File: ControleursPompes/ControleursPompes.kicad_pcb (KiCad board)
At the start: 4 copper layers, 90.8 x 49.5 mm, 91 parts, among them J1 SWD, J10 EV, J11 VACUOSTAT, J12 PV, J13 EV, J14 VACUOSTAT, J15 PV, J16 EV, J17 VACUOSTAT, J2 PWR_IN, J3 I2C 5V, J4 I2C 3.3V, J5 ARIG Interf, J6 PV, J7 EV, J8 VACUOSTAT, J9 PV, Q1 BSS138, Q2 BSS138, SW1 Reset, SW2 Reset, SW3 Reset, U1 AMS1117-3.3, U2 STM32F103C8Tx, U3 TB6612FNG, U4 TB6612FNG, U5 TB6612FNG, U6 TB6612FNG, Y1 16Mhz

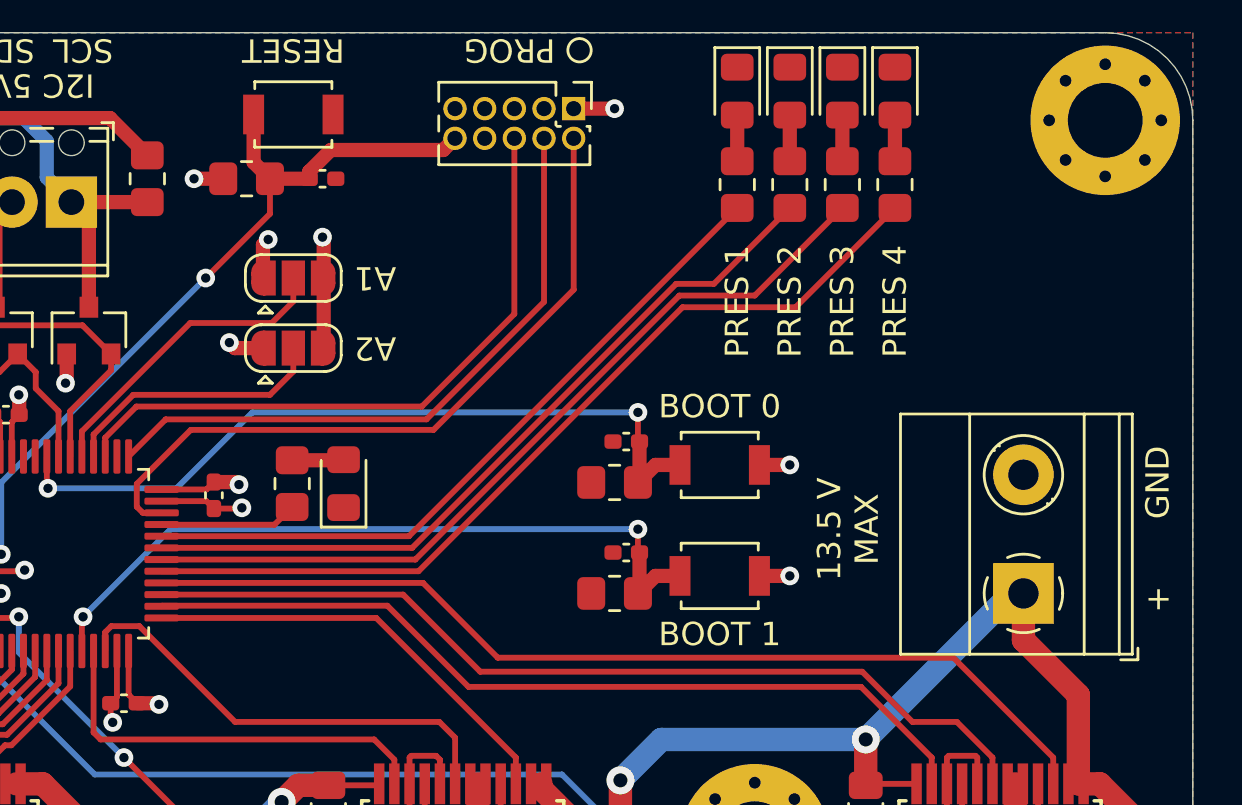
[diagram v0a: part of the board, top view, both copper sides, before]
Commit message: Ajout bornier alim 5V sur controleur pompes
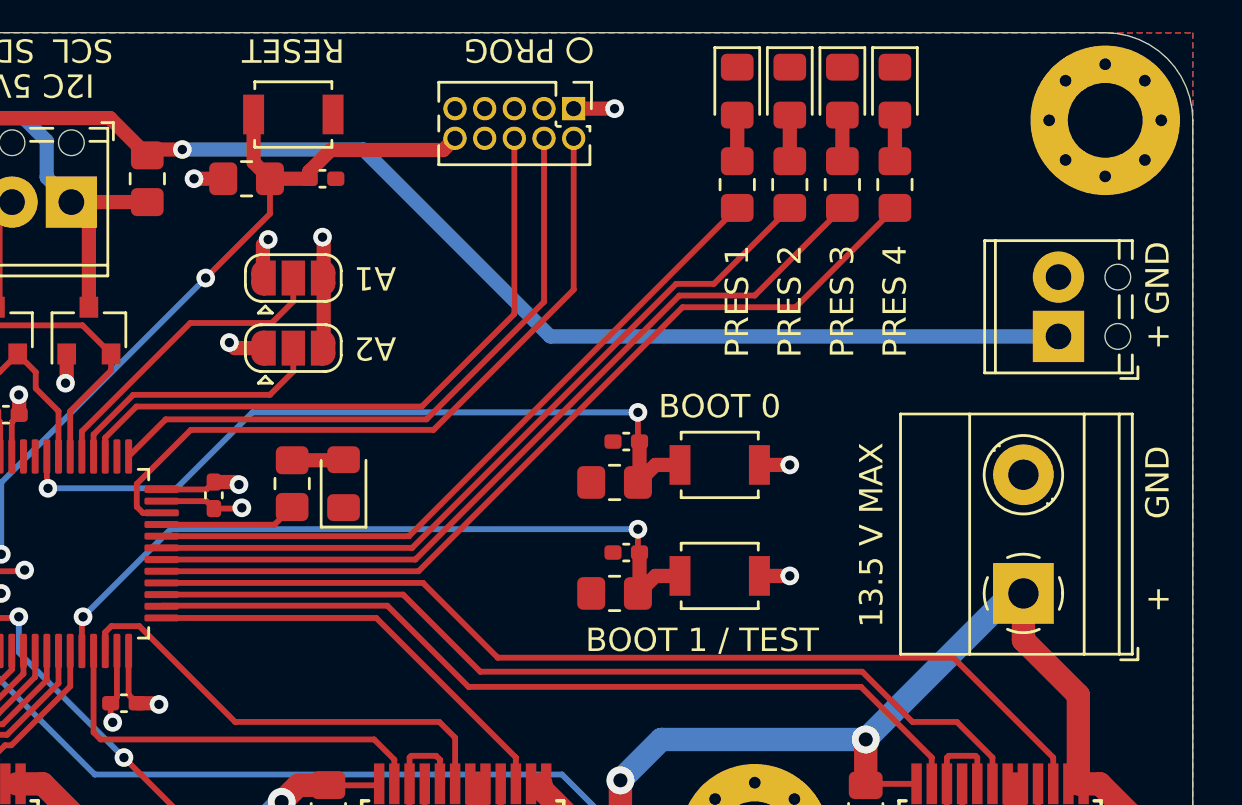
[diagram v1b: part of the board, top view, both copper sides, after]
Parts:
- added J18: Alim 5V, TerminalBlock_Phoenix:TerminalBlock_Phoenix_MPT-0,5-2-2.54_1x02_P2.54mm_Horizontal, F.Cu at (185.0, 84.8)
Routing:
- net +5V: track 52.2 -> 94.6 mm, vias 0 -> 1
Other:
- board text added: "BOOT 1 / TEST"
- board text removed: "BOOT 1"

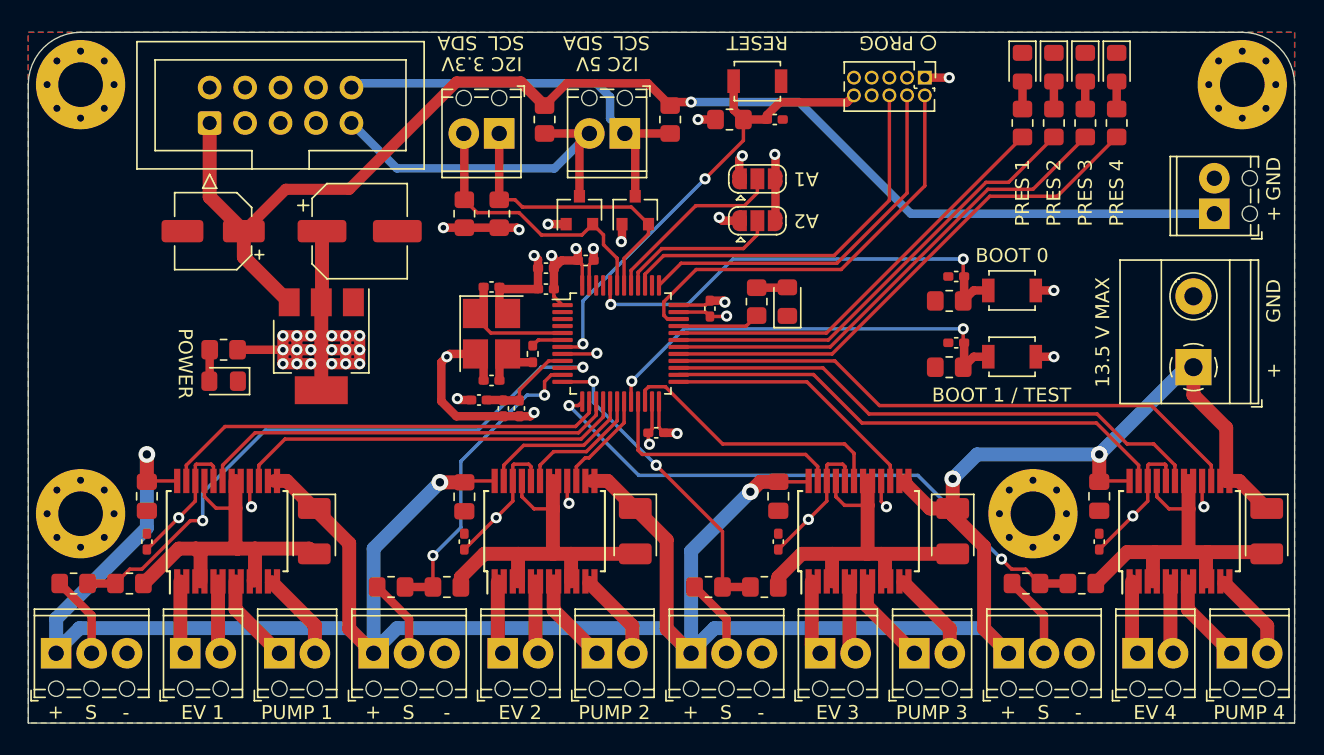
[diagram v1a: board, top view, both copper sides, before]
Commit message: Ajout 4 inputs TOR sur le contrôleur pompes
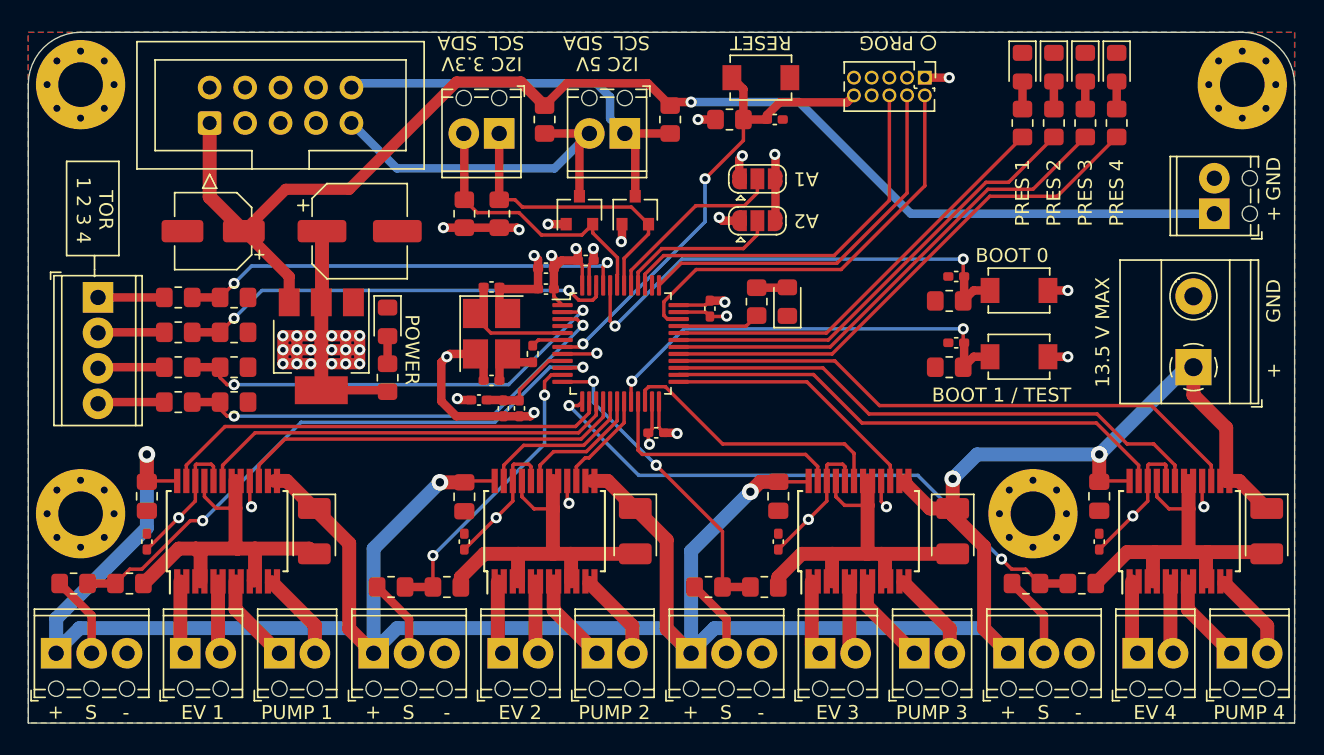
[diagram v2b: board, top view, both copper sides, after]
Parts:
- added J19: TOR, TerminalBlock_Phoenix:TerminalBlock_Phoenix_MPT-0,5-4-2.54_1x04_P2.54mm_Horizontal, F.Cu at (105.0, 90.8)
- added R23: 2.4k, Resistor_SMD:R_0805_2012Metric_Pad1.20x1.40mm_HandSolder, F.Cu at (110.8, 90.8)
- added R24: 4.7k, Resistor_SMD:R_0805_2012Metric_Pad1.20x1.40mm_HandSolder, F.Cu at (114.8, 90.8)
- added R25: 2.4k, Resistor_SMD:R_0805_2012Metric_Pad1.20x1.40mm_HandSolder, F.Cu at (110.8, 93.2)
- added R26: 4.7k, Resistor_SMD:R_0805_2012Metric_Pad1.20x1.40mm_HandSolder, F.Cu at (114.8, 93.2)
- added R27: 2.4k, Resistor_SMD:R_0805_2012Metric_Pad1.20x1.40mm_HandSolder, F.Cu at (110.8, 95.8)
- added R28: 4.7k, Resistor_SMD:R_0805_2012Metric_Pad1.20x1.40mm_HandSolder, F.Cu at (114.8, 95.8)
- added R29: 2.4k, Resistor_SMD:R_0805_2012Metric_Pad1.20x1.40mm_HandSolder, F.Cu at (110.8, 98.2)
- added R30: 4.7k, Resistor_SMD:R_0805_2012Metric_Pad1.20x1.40mm_HandSolder, F.Cu at (114.8, 98.2)
- D3, D4, D5, D6: value Green -> Yellow
- R11, R14, R17, R20: value 33 -> 150
- R5, R8: value 33 -> 68
- SW1, SW2, SW3: footprint Button_Switch_SMD:SW_SPST_B3U-1000P -> ARIG:SW_TS_1088_AR_3x4x2
- moved D1 12.5 mm to (125.8, 92.5), turned to 270 degrees
- moved R5 11.9 mm to (125.8, 96.5), turned to 90 degrees
- moved SW1 0.50 mm to (171.0, 90.2)
- moved SW3 0.50 mm to (171.0, 95.0)
- moved SW2 0.35 mm to (152.5, 75.0)
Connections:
- U2 pad 2: Net-(U2-Pad2) -> TOR_3
- U2 pad 3: Net-(U2-Pad3) -> TOR_4
- U2 pad 45: Net-(U2-Pad45) -> TOR_1
- U2 pad 46: Net-(U2-Pad46) -> TOR_2
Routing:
- net TOR_4: track 0.00 -> 33.0 mm, vias 0 -> 2
- net TOR_3: track 0.00 -> 32.7 mm, vias 0 -> 2
- net TOR_1: track 0.00 -> 32.5 mm, vias 0 -> 2
- net TOR_2: track 0.00 -> 31.4 mm, vias 0 -> 2
- net Net-(J19-Pad4): track 0.00 -> 4.80 mm
- net Net-(J19-Pad3): track 0.00 -> 4.78 mm
- net Net-(J19-Pad2): track 0.00 -> 4.77 mm
- net Net-(J19-Pad1): track 0.00 -> 4.75 mm
- net +3V3: track 121.3 -> 123.6 mm
- net BOOT0: track 33.1 -> 35.3 mm
- net VAC_1: track 44.6 -> 43.4 mm
- net VAC_2: track 22.2 -> 21.5 mm
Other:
- board text added: "TOR 1 2 3 4"

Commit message: Erreur entre la sérigraphie et l'assignation des PIN
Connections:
- R11 pad 1: PRES_4 -> PRES_1
- R14 pad 1: PRES_3 -> PRES_2
- R17 pad 1: PRES_2 -> PRES_3
- R20 pad 1: PRES_1 -> PRES_4
- U2 pad 29: PRES_1 -> PRES_4
- U2 pad 30: PRES_2 -> PRES_3
- U2 pad 31: PRES_3 -> PRES_2
- U2 pad 32: PRES_4 -> PRES_1
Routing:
- net PRES_4: track 30.5 -> 37.8 mm
- net PRES_1: track 37.8 -> 30.5 mm
- net PRES_3: track 32.9 -> 35.4 mm
- net PRES_2: track 35.4 -> 32.9 mm

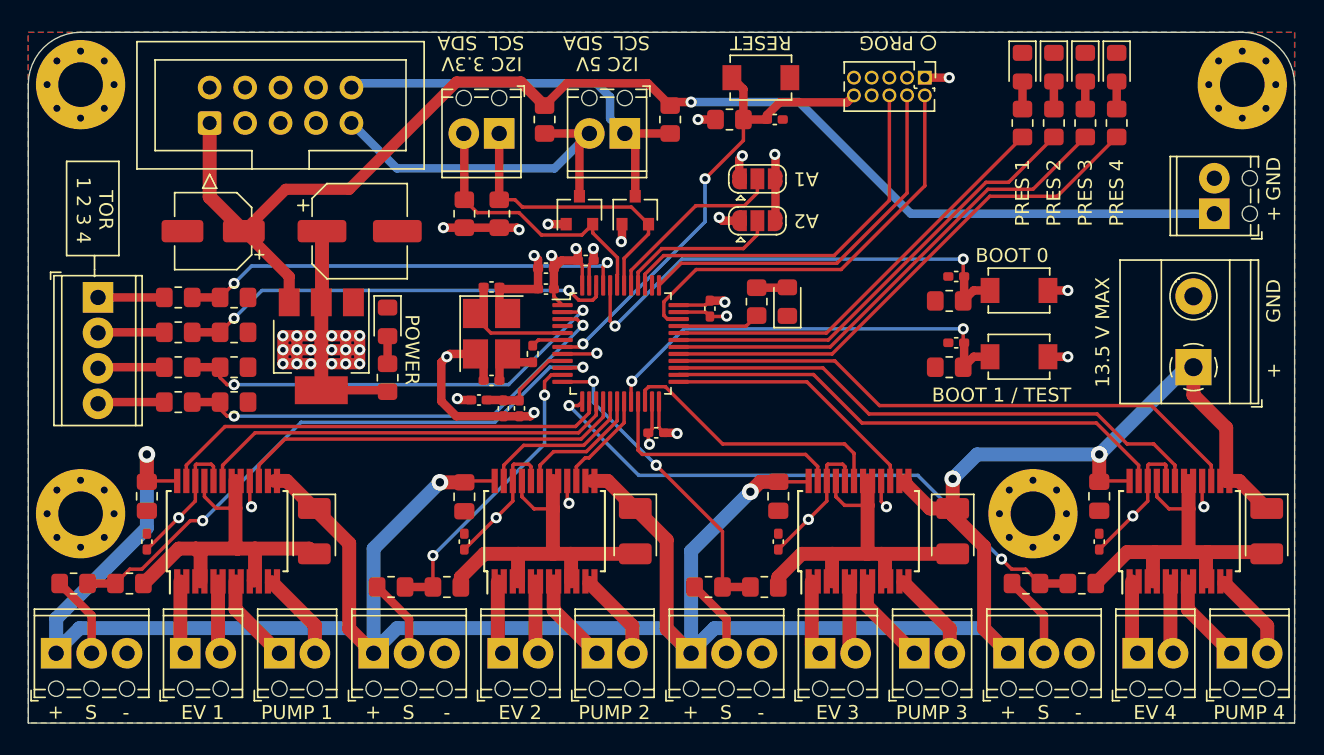
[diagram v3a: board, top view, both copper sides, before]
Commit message: Upgrade vacuum controller
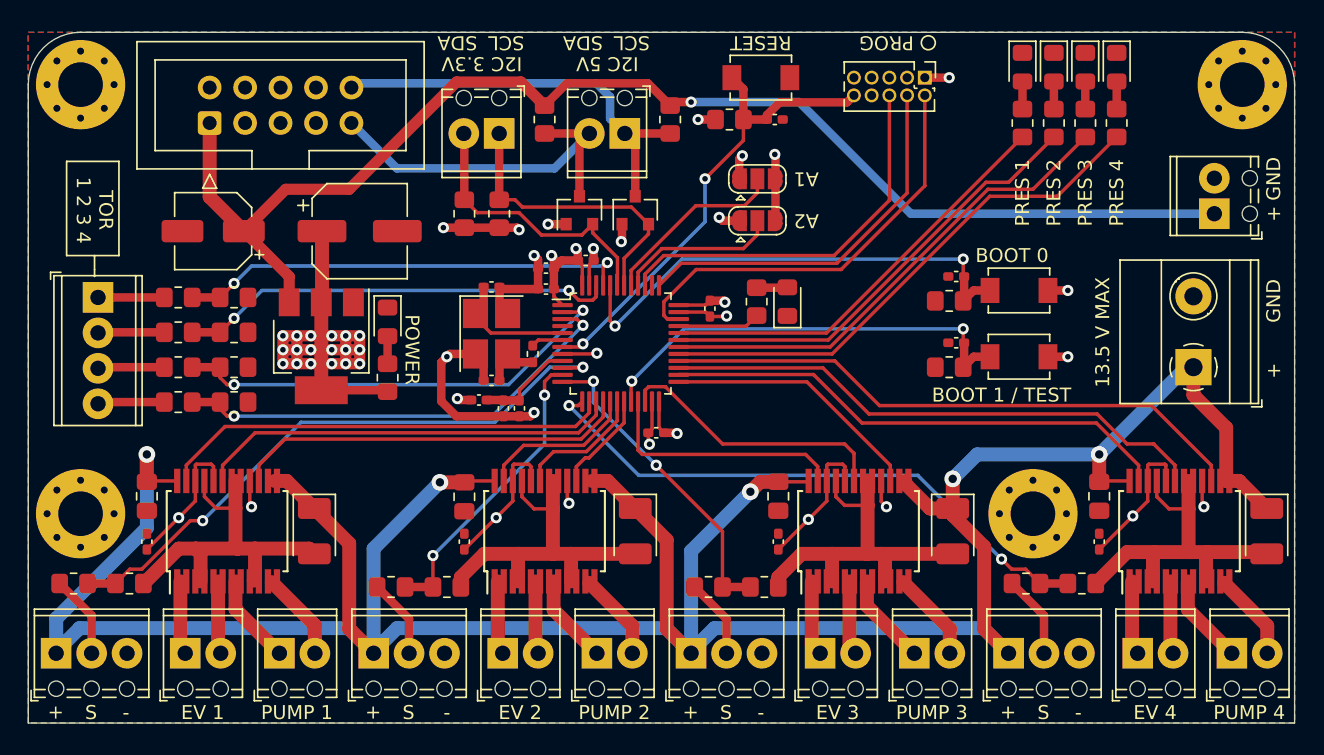
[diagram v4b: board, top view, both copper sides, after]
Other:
- net class Default removed
